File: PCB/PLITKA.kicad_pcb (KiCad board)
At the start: 2 copper layers, 120.5 x 85.5 mm, 47 parts, among them SW1 SW_DPDT_x2, SW10 MX_SW_HS, SW11 MX_SW_HS, SW12 MX_SW_HS, SW13 MX_SW_HS, SW14 MX_SW_HS, SW15 MX_SW_HS, SW16 MX_SW_HS, SW17 MX_SW_HS, SW18 MX_SW_HS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

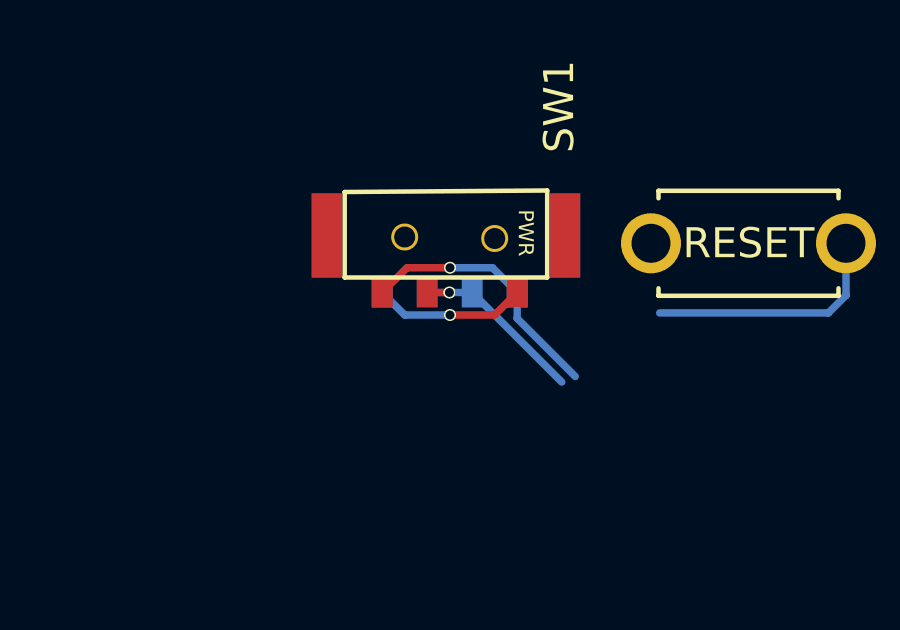
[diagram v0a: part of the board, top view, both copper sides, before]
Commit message: Orphan via removal
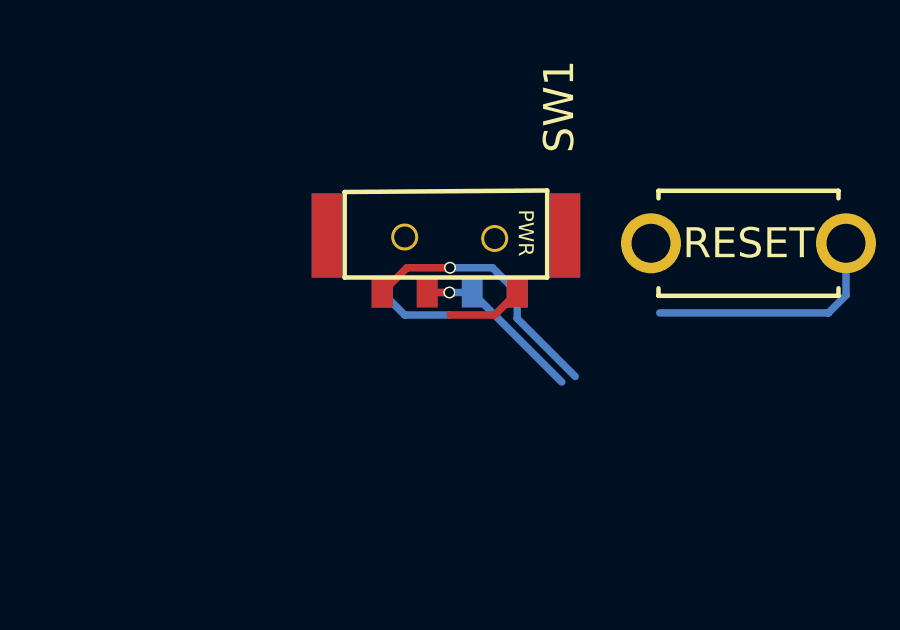
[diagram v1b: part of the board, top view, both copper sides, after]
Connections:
- U1 pad 13: +BATT -> unconnected-(U1-VBAT-Pad13)
- U1 pad 16: VCC -> +BATT
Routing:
- net (no net): vias 1 -> 0
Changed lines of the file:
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@@
 			(layer "B.SilkS")
 		)
-		(pad "" smd rect
-			(at 1.3 -0.1 270)
-			(size 2.8 1)
-			(property pad_prop_mechanical)
-			(layers "F.Cu" "F.Mask" "F.Paste")
-		)
-		(pad "" smd rect
-			(at 1.3 -0.1 270)
-			(size 2.8 1)
-			(property pad_prop_mechanical)
-			(layers "B.Cu" "B.Mask" "B.Paste")
-		)
-		(pad "" smd rect
-			(at 1.3 7.85 270)
-			(size 2.8 1)
-			(property pad_prop_mechanical)
-			(layers "F.Cu" "F.Mask" "F.Paste")
-		)
-		(pad "" smd rect
-			(at 1.3 7.85 270)
-			(size 2.8 1)
-			(property pad_prop_mechanical)
-			(layers "B.Cu" "B.Mask" "B.Paste")
-		)
 		(pad "" np_thru_hole circle
 			(at 1.35 5.25 270)
@@
 			(pintype "passive")
 		)
+		(pad "NC" smd rect
+			(at 1.3 -0.1 270)
+			(size 2.8 1)
+			(property pad_prop_mechanical)
+			(layers "F.Cu" "F.Mask" "F.Paste")
+		)
+		(pad "NC" smd rect
+			(at 1.3 -0.1 270)
+			(size 2.8 1)
+			(property pad_prop_mechanical)
+			(layers "B.Cu" "B.Mask" "B.Paste")
+		)
+		(pad "NC" smd rect
+			(at 1.3 7.85 270)
+			(size 2.8 1)
+			(property pad_prop_mechanical)
+			(layers "F.Cu" "F.Mask" "F.Paste")
+		)
+		(pad "NC" smd rect
+			(at 1.3 7.85 270)
+			(size 2.8 1)
+			(property pad_prop_mechanical)
+			(layers "B.Cu" "B.Mask" "B.Paste")
+		)
 		(embedded_fonts no)
 	)
@@
 			(unit
 				(name "A")
-				(pins "1" "2" "3" "4" "5" "6" "7" "8" "9" "10" "11" "12" "13" "14" "15"
-					"16" "17" "18" "19" "20" "21" "22" "23" "24"
+				(pins "1" "2" "3" "4" "5" "6" "7" "8" "9" "10" "11" "12" "16" "14" "13"
+					"15" "17" "18" "19" "20" "21" "22" "23" "24"
 				)
 			)
@@
 			(layers "*.Cu" "*.SilkS" "*.Mask")
 			(remove_unused_layers no)
-			(net "+BATT")
+			(net "unconnected-(U1-VBAT-Pad13)")
 			(pinfunction "VBAT_13")
-			(pintype "power_out")
+			(pintype "power_out+no_connect")
 		)
 		(pad "14" thru_hole circle
@@
 			(layers "*.Cu" "*.SilkS" "*.Mask")
 			(remove_unused_layers no)
-			(net "VCC")
+			(net "+BATT")
 			(pinfunction "EXT_VCC_16")
 			(pintype "power_in")
@@
 		(net "")
 	)
-	(via
-		(at 109.65 36.37)
-		(size 0.4)
-		(drill 0.3)
-		(layers "F.Cu" "B.Cu")
-		(capping no)
-		(covering
-			(front no)
-			(back no)
-		)
-		(plugging
-			(front no)
-			(back no)
-		)
-		(filling no)
-		(net "")
-	)
